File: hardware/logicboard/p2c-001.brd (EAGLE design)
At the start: 89 x 51 mm, 53 parts, among them IC1 74LS06N, J0 9V, J1 MKR, J11 Qwiic, J2 GPIO, J4 RLY, J5 SPI, J7 DIN5, J9 DIN5, K1 G5V1, Q11 220mA/50V/3.5Ω, Q12 220mA/50V/3.5Ω, T1 2SC1815, U1 DS18B20

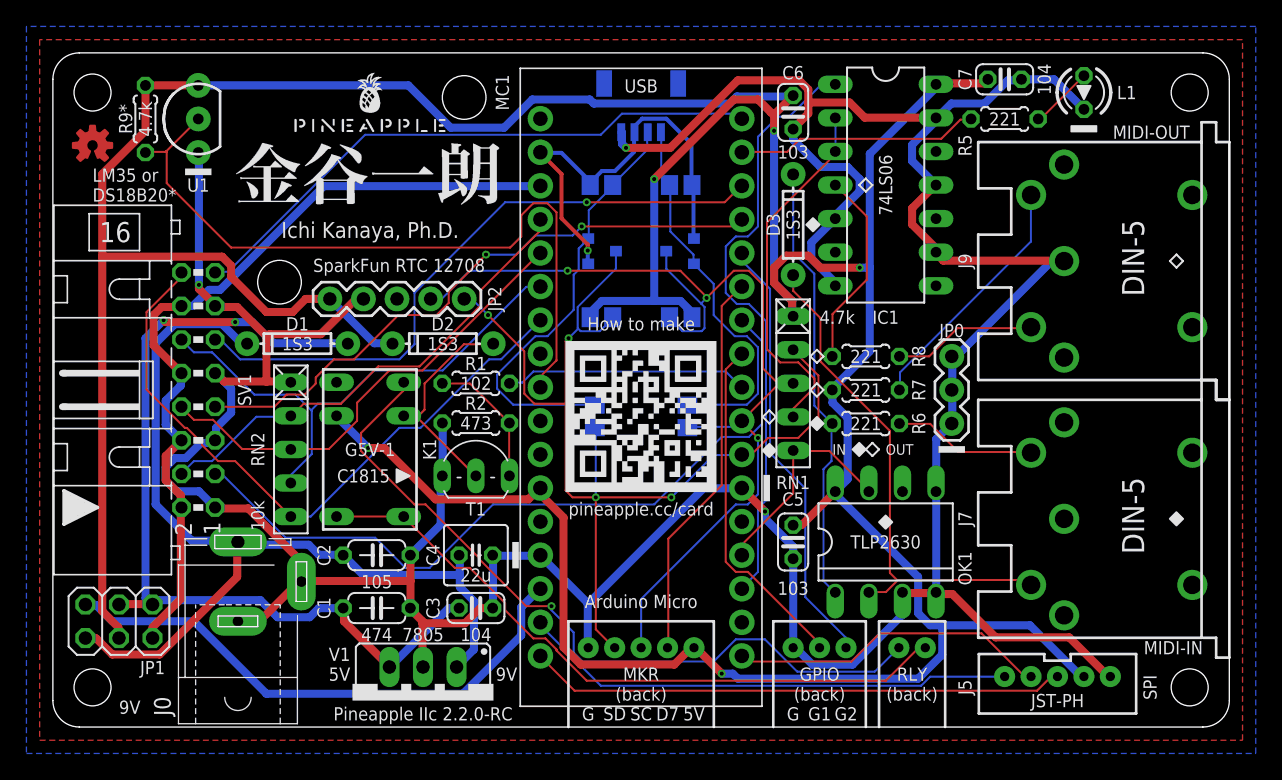
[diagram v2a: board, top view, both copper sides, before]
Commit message: Renumbered parts.
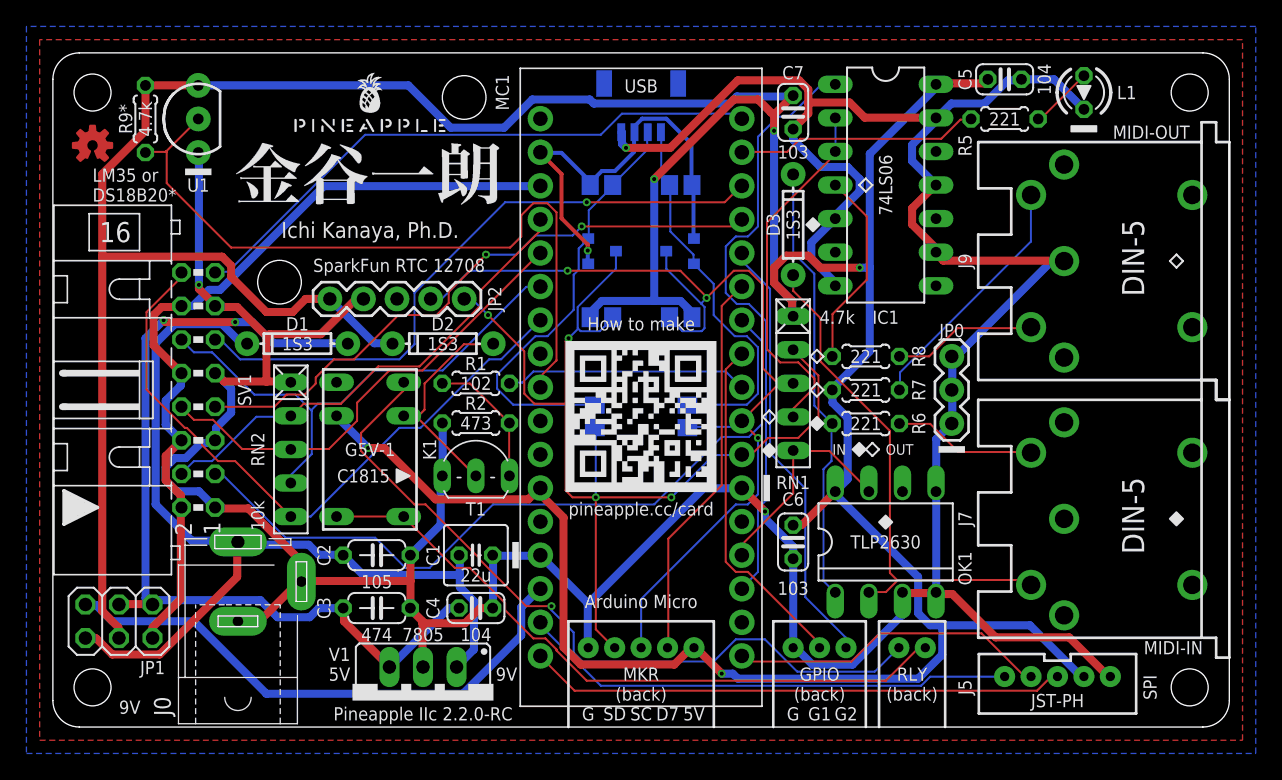
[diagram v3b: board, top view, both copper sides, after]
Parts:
- C1: value 1u -> 22u; device rcl:C050-024X044 -> rcl:C025-050X050
- C3: value 0.1u -> 1u; device rcl:C025-024X044 -> rcl:C050-024X044
- C4: value 22u -> 0.1u; device rcl:C025-050X050 -> rcl:C025-024X044
- C5: value 0.01u -> 0.1u; device resistor:C025-024X044 -> rcl:C025-024X044
- C7: value 0.1u -> 0.01u; device rcl:C025-024X044 -> resistor:C025-024X044
- moved C5 38.5 mm to (72.0, 49.0), turned to 0 degrees
- moved C6 32.5 mm to (56.0, 14.0)
- moved C7 16.2 mm to (56.0, 46.5), turned to 270 degrees
- moved C1 8.50 mm to (32.0, 13.0)
- moved C3 7.50 mm to (24.5, 9.00)
- moved C4 4.00 mm to (32.0, 9.00)
- renumbered Q11 to Q1, Q12 to Q2
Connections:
- net V+: now also C1.1; no longer C4.1
- net VOUT: now also C4.1; no longer C1.1
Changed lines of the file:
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@@
 <attribute name="VALUE" x="-0.43" y="25.4746" size="1.778" layer="27" ratio="10" rot="R90"/>
 </element>
-<element name="C4" library="rcl" library_urn="urn:adsk.eagle:library:334" package="C025-050X050" package3d_urn="urn:adsk.eagle:package:23633/1" value="22u" x="32" y="13" smashed="yes">
+<element name="C1" library="rcl" library_urn="urn:adsk.eagle:library:334" package="C025-050X050" package3d_urn="urn:adsk.eagle:package:23633/1" value="22u" x="32" y="13" smashed="yes">
 <attribute name="NAME" x="29.25" y="13" size="1" layer="25" ratio="10" rot="R90" align="bottom-center"/>
 <attribute name="POPULARITY" value="16" x="32" y="13" size="1.778" layer="27" display="off"/>
@@
 <attribute name="VALUE" x="22.722" y="10.333" size="1.27" layer="27" ratio="10"/>
 </element>
-<element name="C1" library="rcl" library_urn="urn:adsk.eagle:library:334" package="C050-024X044" package3d_urn="urn:adsk.eagle:package:23643/1" value="1u" x="24.5" y="9" smashed="yes">
+<element name="C3" library="rcl" library_urn="urn:adsk.eagle:library:334" package="C050-024X044" package3d_urn="urn:adsk.eagle:package:23643/1" value="1u" x="24.5" y="9" smashed="yes">
 <attribute name="NAME" x="21" y="9" size="1" layer="25" ratio="10" rot="R90" align="bottom-center"/>
 <attribute name="POPULARITY" value="33" x="24.5" y="9" size="1.778" layer="27" display="off"/>
@@
 <attribute name="VALUE" x="22.722" y="6.333" size="1.27" layer="27" ratio="10"/>
 </element>
-<element name="C3" library="rcl" library_urn="urn:adsk.eagle:library:334" package="C025-024X044" package3d_urn="urn:adsk.eagle:package:23630/1" value="0.1u" x="32" y="9" smashed="yes">
+<element name="C4" library="rcl" library_urn="urn:adsk.eagle:library:334" package="C025-024X044" package3d_urn="urn:adsk.eagle:package:23630/1" value="0.1u" x="32" y="9" smashed="yes">
 <attribute name="NAME" x="29.25" y="9" size="1" layer="25" ratio="10" rot="R90" align="bottom-center"/>
 <attribute name="POPULARITY" value="56" x="32" y="9" size="1.778" layer="27" display="off"/>
@@
 <attribute name="VALUE" x="30.222" y="6.333" size="1.27" layer="27" ratio="10"/>
 </element>
-<element name="C6" library="resistor" library_urn="urn:adsk.eagle:library:348" package="C025-024X044" package3d_urn="urn:adsk.eagle:package:23630/1" value="0.01u" x="56" y="46.5" smashed="yes" rot="R270">
+<element name="C7" library="resistor" library_urn="urn:adsk.eagle:library:348" package="C025-024X044" package3d_urn="urn:adsk.eagle:package:23630/1" value="0.01u" x="56" y="46.5" smashed="yes" rot="R270">
 <attribute name="NAME" x="56" y="49" size="1" layer="25" ratio="10" align="bottom-center"/>
 <attribute name="VALUE" x="53.333" y="48.278" size="1.27" layer="27" ratio="10" rot="R270"/>
 </element>
-<element name="C5" library="resistor" library_urn="urn:adsk.eagle:library:348" package="C025-024X044" package3d_urn="urn:adsk.eagle:package:23630/1" value="0.01u" x="56" y="14" smashed="yes" rot="R270">
+<element name="C6" library="resistor" library_urn="urn:adsk.eagle:library:348" package="C025-024X044" package3d_urn="urn:adsk.eagle:package:23630/1" value="0.01u" x="56" y="14" smashed="yes" rot="R270">
 <attribute name="NAME" x="56" y="16.75" size="1" layer="25" ratio="10" align="bottom-center"/>
 <attribute name="VALUE" x="53.333" y="15.778" size="1.27" layer="27" ratio="10" rot="R270"/>
@@
 <attribute name="VALUE" x="46.865" y="43.54" size="1.27" layer="28" rot="MR180"/>
 </element>
-<element name="Q11" library="SparkFun-DiscreteSemi" library_urn="urn:adsk.eagle:library:514" package="SOT23-3" package3d_urn="urn:adsk.eagle:package:38446/1" value="220mA/50V/3.5Ω" x="47.5" y="36" smashed="yes" rot="MR270">
+<element name="Q1" library="SparkFun-DiscreteSemi" library_urn="urn:adsk.eagle:library:514" package="SOT23-3" package3d_urn="urn:adsk.eagle:package:38446/1" value="220mA/50V/3.5Ω" x="47.5" y="36" smashed="yes" rot="MR270">
 <attribute name="NAME" x="49.5" y="36" size="1" layer="26" ratio="20" rot="MR90" align="bottom-center"/>
 <attribute name="PROD_ID" value="TRANS-00830" x="47.5" y="36" size="1.778" layer="28" rot="MR270" display="off"/>
 <attribute name="VALUE" x="47.5" y="34.349" size="0.6096" layer="28" font="vector" ratio="20" rot="MR0" align="top-center"/>
 </element>
-<element name="Q12" library="SparkFun-DiscreteSemi" library_urn="urn:adsk.eagle:library:514" package="SOT23-3" package3d_urn="urn:adsk.eagle:package:38446/1" value="220mA/50V/3.5Ω" x="41.5" y="36" smashed="yes" rot="MR90">
+<element name="Q2" library="SparkFun-DiscreteSemi" library_urn="urn:adsk.eagle:library:514" package="SOT23-3" package3d_urn="urn:adsk.eagle:package:38446/1" value="220mA/50V/3.5Ω" x="41.5" y="36" smashed="yes" rot="MR90">
 <attribute name="NAME" x="39.5" y="36" size="1" layer="26" ratio="20" rot="MR90" align="top-center"/>
 <attribute name="PROD_ID" value="TRANS-00830" x="41.5" y="36" size="1.778" layer="28" rot="MR90" display="off"/>
@@
 <attribute name="VALUE" x="63.73" y="3.27" size="0.6096" layer="28" font="vector" ratio="20" rot="MR180"/>
 </element>
-<element name="C7" library="rcl" library_urn="urn:adsk.eagle:library:334" package="C025-024X044" package3d_urn="urn:adsk.eagle:package:23630/1" value="0.1u" x="72" y="49" smashed="yes">
+<element name="C5" library="rcl" library_urn="urn:adsk.eagle:library:334" package="C025-024X044" package3d_urn="urn:adsk.eagle:package:23630/1" value="0.1u" x="72" y="49" smashed="yes">
 <attribute name="NAME" x="69.5" y="49" size="1" layer="25" ratio="10" rot="R90" align="bottom-center"/>
 <attribute name="POPULARITY" value="56" x="72" y="49" size="1.778" layer="27" display="off"/>
@@
 <contactref element="IC1" pad="5"/>
 <contactref element="V1" pad="GND"/>
+<contactref element="C4" pad="2"/>
 <contactref element="C3" pad="2"/>
+<contactref element="C2" pad="2"/>
 <contactref element="C1" pad="2"/>
-<contactref element="C2" pad="2"/>
-<contactref element="C4" pad="2"/>
-<contactref element="C5" pad="2"/>
 <contactref element="C6" pad="2"/>
+<contactref element="C7" pad="2"/>
 <contactref element="T1" pad="E"/>
 <contactref element="R2" pad="1"/>
 <contactref element="U1" pad="1"/>
-<contactref element="C7" pad="2"/>
+<contactref element="C5" pad="2"/>
 <contactref element="JP0" pad="1"/>
 <contactref element="JP0" pad="3"/>
@@
 <contactref element="R203" pad="2"/>
 <contactref element="R201" pad="2"/>
-<contactref element="C5" pad="1"/>
 <contactref element="C6" pad="1"/>
 <contactref element="C7" pad="1"/>
+<contactref element="C5" pad="1"/>
 <contactref element="J1" pad="5"/>
 <contactref element="U1" pad="3"/>
@@
 <contactref element="U$2" pad="P$33"/>
 <contactref element="J11" pad="2"/>
-<contactref element="Q12" pad="1"/>
+<contactref element="Q2" pad="1"/>
 <contactref element="R204" pad="2"/>
-<contactref element="Q11" pad="1"/>
+<contactref element="Q1" pad="1"/>
 <contactref element="R202" pad="2"/>
 <wire x1="40.4622" y1="36.0426" x2="40.4622" y2="35.052" width="0.3048" layer="16"/>
@@
 <signal name="SCL">
 <contactref element="U$2" pad="P$10"/>
-<contactref element="Q11" pad="3"/>
+<contactref element="Q1" pad="3"/>
 <contactref element="R201" pad="1"/>
 <contactref element="RZ1" pad="1"/>
@@
 <contactref element="U$2" pad="P$11"/>
 <contactref element="R203" pad="1"/>
-<contactref element="Q12" pad="3"/>
+<contactref element="Q2" pad="3"/>
 <contactref element="RZ2" pad="1"/>
 <contactref element="J1" pad="2"/>
@@
 <contactref element="J11" pad="4"/>
 <contactref element="R202" pad="1"/>
-<contactref element="Q11" pad="2"/>
+<contactref element="Q1" pad="2"/>
 <contactref element="RZ1" pad="2"/>
 <wire x1="48.4632" y1="35.7378" x2="48.4632" y2="35.052" width="0.1524" layer="16"/>
@@
 <contactref element="J11" pad="3"/>
 <contactref element="R204" pad="1"/>
-<contactref element="Q12" pad="2"/>
+<contactref element="Q2" pad="2"/>
 <contactref element="RZ2" pad="2"/>
 <wire x1="40.5384" y1="39.0906" x2="40.5384" y2="36.957" width="0.1524" layer="16"/>
@@
 <contactref element="C2" pad="1"/>
 <contactref element="D1" pad="C"/>
-<contactref element="C4" pad="1"/>
+<contactref element="C1" pad="1"/>
 <contactref element="V1" pad="IN"/>
 <contactref element="J0" pad="3"/>
@@
 <signal name="VOUT" class="2">
 <contactref element="V1" pad="OUT"/>
+<contactref element="C4" pad="1"/>
 <contactref element="C3" pad="1"/>
-<contactref element="C1" pad="1"/>
 <contactref element="D1" pad="A"/>
 <contactref element="JP1" pad="4"/>

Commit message: L1->L2.
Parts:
- renumbered L1 to L2
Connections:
- net LED1 renamed LED2
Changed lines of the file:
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@@
 <attribute name="VALUE" x="74.1336" y="48.3114" size="0.9906" layer="27" ratio="10" rot="R180"/>
 </element>
-<element name="L1" library="led" library_urn="urn:adsk.eagle:library:259" package="LED3MM" package3d_urn="urn:adsk.eagle:package:15797/1" value="Green" x="78" y="48" smashed="yes" rot="R270">
+<element name="L2" library="led" library_urn="urn:adsk.eagle:library:259" package="LED3MM" package3d_urn="urn:adsk.eagle:package:15797/1" value="Green" x="78" y="48" smashed="yes" rot="R270">
 <attribute name="NAME" x="80.5" y="48" size="1" layer="25" ratio="10" align="center-left"/>
 <attribute name="POPULARITY" value="97" x="78" y="48" size="1.778" layer="27" rot="R270" display="off"/>
@@
 <contactref element="JP0" pad="2"/>
 <contactref element="U$2" pad="P$12"/>
-<contactref element="L1" pad="K"/>
+<contactref element="L2" pad="K"/>
 <contactref element="RN2" pad="1"/>
 <contactref element="U$2" pad="P$21"/>
@@
 <wire x1="52.0446" y1="46.0248" x2="52.12" y2="46.02" width="0.1524" layer="16"/>
 </signal>
-<signal name="LED1">
+<signal name="LED2">
 <contactref element="U$2" pad="P$2"/>
 <contactref element="R5" pad="2"/>
@@
 </signal>
 <signal name="LED1A">
-<contactref element="L1" pad="A"/>
+<contactref element="L2" pad="A"/>
 <contactref element="R5" pad="1"/>
 <wire x1="74.7522" y1="46.0248" x2="74.5998" y2="46.0248" width="0.1524" layer="1"/>

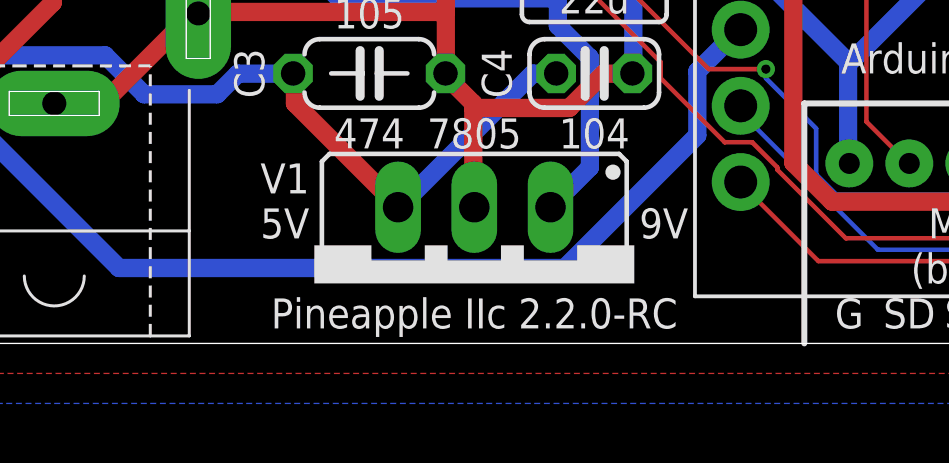
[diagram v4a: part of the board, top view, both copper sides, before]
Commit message: Renamed signals for compatibility with Pineapple II 2.4.0 series.
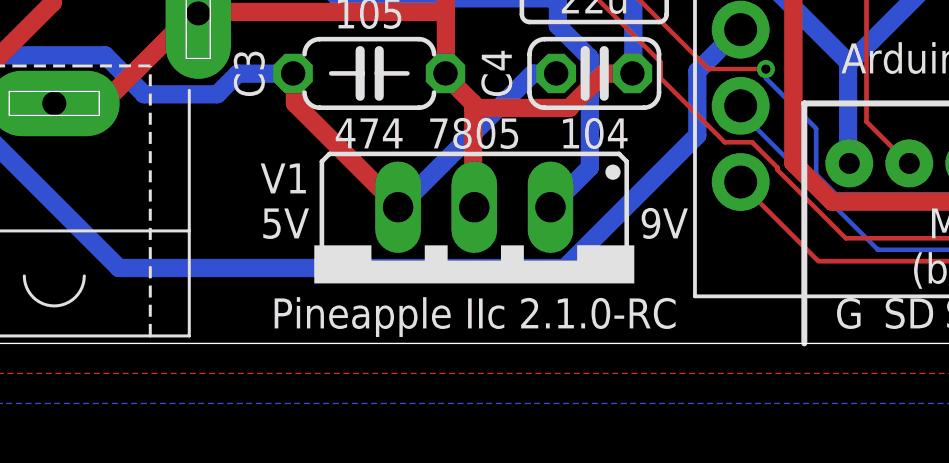
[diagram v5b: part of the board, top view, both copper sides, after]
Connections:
- net A4 renamed MNTR
- net D7 renamed D7GATE
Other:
- board text added: "Pineapple IIc 2.1.0-RC"
- board text removed: "Pineapple IIc 2.2.0-RC"
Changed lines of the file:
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@@
 <text x="31.115" y="33.655" size="1" layer="26" rot="MR90" align="center-left">SDA</text>
 <text x="19.685" y="34.925" size="1" layer="25" align="center-left">SparkFun RTC 12708</text>
-<text x="28" y="0.5" size="1" layer="25" align="bottom-center">Pineapple IIc 2.2.0-RC</text>
+<text x="28" y="0.5" size="1" layer="25" align="bottom-center">Pineapple IIc 2.1.0-RC</text>
 <rectangle x1="34.75" y1="12" x2="35.25" y2="14" layer="22"/>
 <rectangle x1="53.75" y1="17.08" x2="54.25" y2="19.08" layer="22"/>
@@
 <wire x1="17.9832" y1="15.9258" x2="18" y2="15.92" width="0.1524" layer="1"/>
 </signal>
-<signal name="A4">
+<signal name="MNTR">
 <contactref element="U$2" pad="P$27"/>
 </signal>
@@
 <wire x1="52.1208" y1="35.814" x2="52.12" y2="35.86" width="0.1524" layer="16"/>
 </signal>
-<signal name="D7">
+<signal name="D7GATE">
 <contactref element="U$2" pad="P$6"/>
 <contactref element="J1" pad="4"/>
